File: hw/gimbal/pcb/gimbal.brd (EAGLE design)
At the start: 60 x 40 mm, 43 parts

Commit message: Progress on gimbal board.
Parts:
- added C14, C15: 0.01uF, rcl:C0603
- added C16, C17, C20, C21, C22, C23, C24: 0.1uF, rcl:C0603
- added C18, C19: 4.7uF, rcl:C0603
- added C25, C26: 10pF, rcl:C0603
- added R10, R8: 100k, rcl:R0603
- added R11, R9: 10k, rcl:R0603
- added R7: 10, rcl:R0603
- added U$16: (no value), gimbal:CRYSTAL-OSC-SMD-5X3.2
- U$14: value (none) -> 2.2uH
- moved PIMU 12.5 mm to (2.50, 29.0), turned to 270 degrees
- moved PABS 8.56 mm to (2.50, 18.5), turned to 270 degrees
- moved SIMU 2.24 mm to (2.50, 8.00), turned to 270 degrees
- moved U$9 1.97 mm to (8.50, 18.3), turned to 270 degrees
- moved R3 1.60 mm to (50.4, 20.2), turned to 180 degrees
- moved C7 1.50 mm to (38.0, 29.0)
- moved USBO 1.40 mm to (32.0, 24.1)
- moved JP3 1.12 mm to (12.3, 5.50)
- moved JP2 1.02 mm to (38.5, 1.80)
- moved C11 0.85 mm to (45.8, 24.7)
- moved R4 0.78 mm to (48.1, 23.5)
- moved C6 0.70 mm to (42.2, 34.7)
- moved C12 0.58 mm to (50.5, 27.0)
- moved JP1 0.54 mm to (56.0, 1.80)
- moved U$10 0.50 mm to (5.10, 37.3)
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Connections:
- new net BLDC_FAULT1: U$1.51, U$5.18
- new net BLDC_FAULT2: U$1.40, U$6.18
- new net BLDC_RESET/: U$1.4, U$5.16, U$6.16
- new net BLDC_SLEEP/: U$1.3, U$5.17, U$6.17
- new net MOTOR1_EN: U$5.22, U$5.24, U$5.26
- new net MOTOR1_IN1: U$1.37, U$5.27
- new net MOTOR1_IN2: U$1.38, U$5.25
- new net MOTOR1_IN3: U$1.39, U$5.23
- new net MOTOR2_EN: U$6.22, U$6.24, U$6.26
- new net MOTOR2_IN1: U$1.14, U$6.27
- new net MOTOR2_IN2: U$1.15, U$6.25
- new net MOTOR2_IN3: U$1.16, U$6.23
- new net N$23: C18.1, U$1.30
- new net N$24: C24.1, U$1.7, U$9.5
- new net N$25: C14.1, U$6.1
- new net N$26: C14.2, U$6.2
- new net N$27: C15.2, U$5.2
- new net N$28: C15.1, U$5.1
- new net N$29: C16.2, U$5.3
- new net N$30: C17.2, U$6.3
- new net N$31: U$1.49, U$9.2
- new net N$32: U$1.46, U$9.4
- new net N$33: R7.2, U$1.60
- new net N$34: R8.1, R9.2, U$1.9
- new net N$35: C25.1, U$1.5, U$16.1
- new net N$36: C26.1, U$1.6, U$16.3
- new net N$38: R10.1, R11.2, U$1.10
- new net SLAVE_RX: U$1.55, U$8.3
- new net SLAVE_TX: U$1.50, U$8.2
- net +12V: now also C16.1, C17.1, R10.2, U$5.11, U$5.4, U$6.11, U$6.4
- net +3V3: now also C19.1, C20.1, C21.1, C22.1, C23.1, JP3.5, U$1.1, U$1.13, U$1.19, U$1.32, U$1.48, U$1.64, U$9.1
- net +8V: now also R8.2, U$8.4
- net AEG_PWM: now also U$1.26
- net AGITATOR_PWM: now also U$1.27
- net BOOST_EN: now also U$1.52
- net GND: now also C18.2, C19.2, C20.2, C21.2, C22.2, C23.2, C24.2, C25.2, C26.2, R11.1, R7.1, R9.1, U$1.31, U$1.47, U$16.2, U$16.4, U$5.10, U$5.14, U$5.20, U$5.28, U$5.6, U$5.7, U$5.G0, U$5.G1, U$5.G2, U$5.G3, U$5.G4, U$5.G5, U$5.G6, U$5.G7, U$5.G8, U$6.10, U$6.14, U$6.20, U$6.28, U$6.6, U$6.7, U$6.G0, U$6.G1, U$6.G2, U$6.G3, U$6.G4, U$6.G5, U$6.G6, U$6.G7, U$6.G8, U$8.1, U$9.3
- net LASER_EN: now also U$1.28
- net MOTOR_D1: now also U$1.53
- net MOTOR_FB: now also U$1.8
- net MOTOR_SF: now also U$1.2
- net PABS_SCL: now also U$1.41; no longer U$1.61
- net PABS_SDA: now also U$1.61; no longer U$1.62
- net PIMU_SCL: now also U$1.58; no longer U$1.41
- net PIMU_SDA: now also U$1.59; no longer U$1.40
- net SIMU_SDA: now also U$1.62; no longer U$1.55
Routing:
- added copper zone on layer 16, net GND

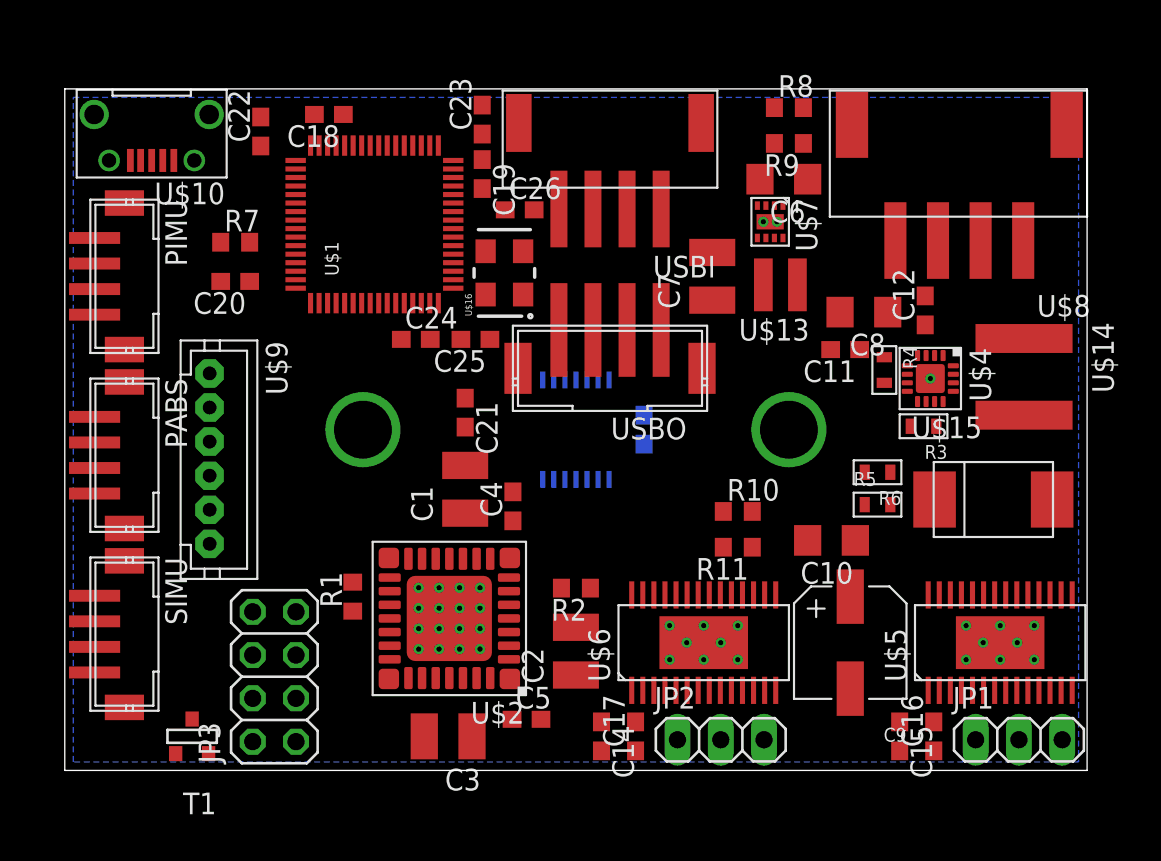
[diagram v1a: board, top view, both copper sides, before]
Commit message: gimbal board: Fix all DRC errors with part placement and library.
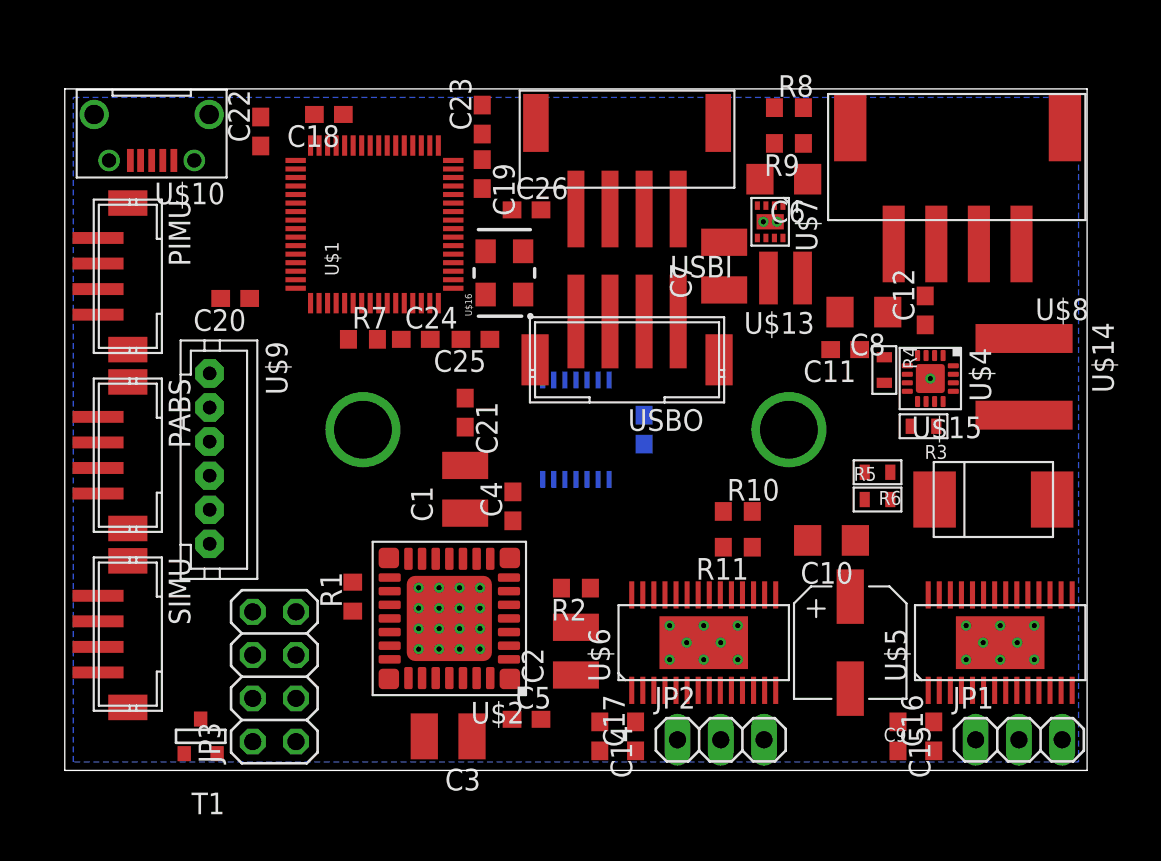
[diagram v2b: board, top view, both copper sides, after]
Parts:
- moved R7 9.42 mm to (17.5, 25.3)
- moved USBO 1.12 mm to (33.0, 24.6)
- moved C20 1.00 mm to (10.0, 27.7)
- moved USBI 1.00 mm to (33.0, 35.7)
- moved C7 0.92 mm to (38.7, 29.6)
- moved T1 0.50 mm to (8.00, 2.00)
- moved U$13 0.50 mm to (42.3, 28.9)
- moved C26 0.40 mm to (27.1, 32.9)
- moved R5 0.30 mm to (47.7, 15.9)
- moved U$8 0.22 mm to (52.4, 35.5)
- moved PABS 0.20 mm to (2.70, 18.5)
- moved PIMU 0.20 mm to (2.70, 29.0)
- moved SIMU 0.20 mm to (2.70, 8.00)
- moved C14 0.10 mm to (31.4, 2.00)
- moved C15 0.10 mm to (48.9, 2.00)

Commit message: gimbal board: Continued work: Updated all resistors and caps to the MF libraries.
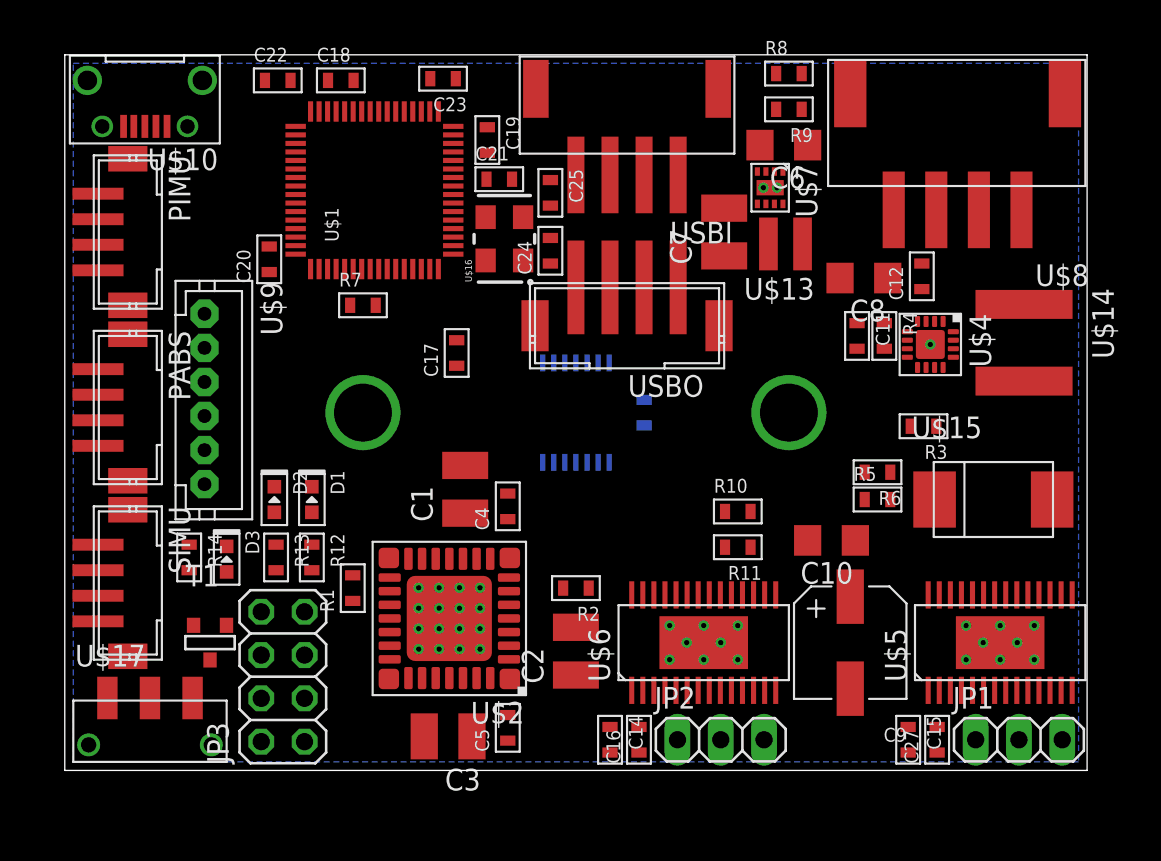
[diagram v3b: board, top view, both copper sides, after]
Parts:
- removed C26: 10pF, rcl:C0603
- added C27: 0.1uF, mfpassives:C0603
- added D1, D2, D3: (no value), mfleds:LED0603
- added R12, R13, R14: 560, mfpassives:R0603
- added U$17: SLIDE_SWITCHJS_SUB_SWITCH, gimbal:JS_SUB_SWITCH
- C11, C12, C13, C14, C15, C16, C17, C18, C19, C20, C21, C22, C23, C25, C4, C5: device rcl:C0603 -> mfpassives:C0603
- C24: value 0.1uF -> 10pF; device rcl:C0603 -> mfpassives:C0603
- R1, R10, R11, R2, R7, R8, R9: device rcl:R0603 -> mfpassives:R0603
- moved C17 24.8 mm to (23.0, 24.5)
- moved C16 17.3 mm to (33.7, 1.80)
- moved C21 13.8 mm to (25.5, 34.7), turned to 0 degrees
- moved C25 9.66 mm to (28.5, 33.9), turned to 270 degrees
- moved C24 9.46 mm to (28.5, 30.5), turned to 90 degrees
- moved T1 5.52 mm to (8.50, 7.50), turned to 0 degrees
- moved U$9 3.51 mm to (8.20, 21.8)
- moved C23 3.32 mm to (22.2, 40.6), turned to 180 degrees
- moved C22 3.16 mm to (12.5, 40.5), turned to 0 degrees
- moved C20 3.05 mm to (12.0, 30.0), turned to 90 degrees
- moved SIMU 3.00 mm to (2.70, 11.0)
- moved PABS 2.80 mm to (2.70, 21.3)
- moved PIMU 2.60 mm to (2.70, 31.6)
- moved C18 2.12 mm to (16.2, 40.5), turned to 0 degrees
- moved U$10 2.04 mm to (4.70, 39.3)
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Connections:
- new net N$37: D2.CATHODE, U$1.35
- new net N$39: D1.ANODE, R12.P$1
- new net N$40: D2.ANODE, R13.P$1
- new net N$41: D3.ANODE, R14.P$1
- new net N$42: D3.CATHODE, U$1.34
- new net N$43: D1.CATHODE, U$1.36
- net +12V: now also C16.P$1, C27.P$1, R10.P$2; no longer C16.1, C17.1, R10.2
- net +3V3: now also C13.P$1, C17.P$1, C19.P$1, C20.P$1, C22.P$1, C23.P$1, R1.P$2, R12.P$2, R13.P$2, R14.P$2, U$17.1; no longer C13.1, C19.1, C20.1, C21.1, C22.1, C23.1, R1.2
- net +8V: now also R8.P$2; no longer R8.2
- net GND: now also C11.P$2, C12.P$2, C13.P$2, C17.P$2, C18.P$2, C19.P$2, C20.P$2, C21.P$2, C22.P$2, C23.P$2, C24.P$2, C25.P$2, C4.P$2, R11.P$1, R2.P$1, R7.P$1, R9.P$1, U$17.3; no longer C11.2, C12.2, C13.2, C18.2, C19.2, C20.2, C21.2, C22.2, C23.2, C24.2, C25.2, C26.2, C4.2, R11.1, R2.1, R7.1, R9.1
- net MOTOR_EN: now also U$1.33, U$17.2
- net MOTOR_FB: now also R2.P$2; no longer R2.2
- net MOTOR_SF: now also R1.P$1; no longer R1.1
- net N$19: now also C11.P$1; no longer C11.1
- net N$21: now also C12.P$1; no longer C12.1
- net N$23: now also C18.P$1; no longer C18.1
- net N$24: now also C21.P$1; no longer C24.1
- net N$25: now also C14.P$1; no longer C14.1
- net N$26: now also C14.P$2; no longer C14.2
- net N$27: now also C15.P$2; no longer C15.2
- net N$28: now also C15.P$1; no longer C15.1
- net N$29: now also C27.P$2; no longer C16.2
- net N$30: now also C16.P$2; no longer C17.2
- net N$33: now also R7.P$2; no longer R7.2
- net N$34: now also R8.P$1, R9.P$2; no longer R8.1, R9.2
- net N$35: now also C24.P$1; no longer C25.1
- net N$36: now also C25.P$1; no longer C26.1
- net N$38: now also R10.P$1, R11.P$2; no longer R10.1, R11.2
- net N$4: now also C4.P$1, C5.P$1; no longer C4.1, C5.1
- net N$5: now also C5.P$2; no longer C5.2
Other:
- board size 60 x 40 mm -> 60 x 42 mm

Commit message: gimbal board: Finish updating the remaining larger caps to the macrofab library versions.
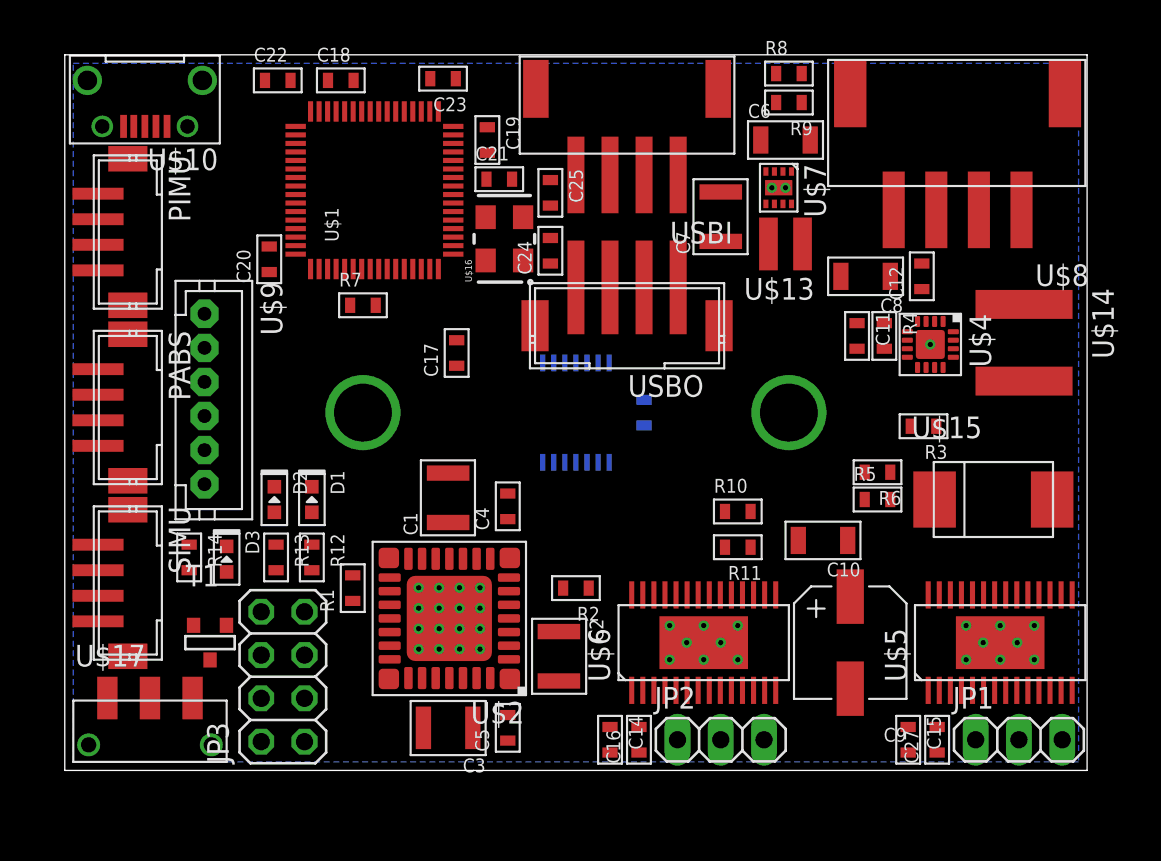
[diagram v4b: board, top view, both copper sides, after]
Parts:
- C1, C2, C3, C7: device rcl:C1210 -> mfpassives:C1210
- C10, C6, C8: device rcl:C1206 -> mfpassives:C1206
- moved C1 1.12 mm to (22.5, 16.0)
- moved C2 1.04 mm to (29.0, 6.70), turned to 270 degrees
- moved C7 0.92 mm to (38.5, 32.5)
- moved C10 0.50 mm to (44.5, 13.5)
- moved C3 0.50 mm to (22.5, 2.50)
- moved U$7 0.50 mm to (41.9, 34.2)
- moved R9 0.40 mm to (42.5, 39.2)
- moved C6 0.32 mm to (42.3, 37.0), turned to 0 degrees
- moved C8 0.14 mm to (47.0, 29.0)
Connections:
- net +12V: now also C10.P$1; no longer C10.1
- net +3V3: now also C7.P$1; no longer C7.1
- net +8V: now also C6.P$1, C8.P$1; no longer C6.1, C8.1
- net GND: now also C1.P$2, C10.P$2, C2.P$2, C3.P$2, C6.P$2, C7.P$2, C8.P$2; no longer C1.2, C10.2, C2.2, C3.2, C6.2, C7.2, C8.2
- net N$4: now also C1.P$1, C2.P$1, C3.P$1; no longer C1.1, C2.1, C3.1

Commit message: gimbal board: Select a few parts, update TODO.
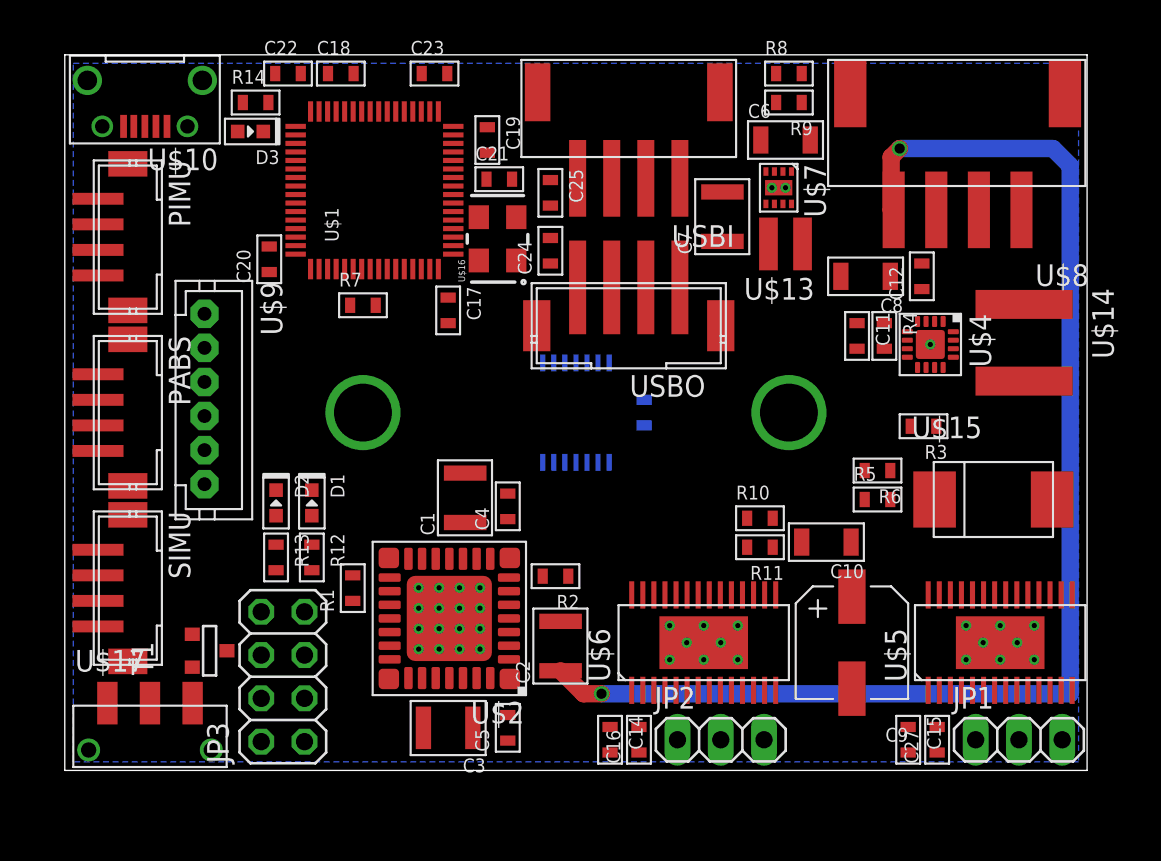
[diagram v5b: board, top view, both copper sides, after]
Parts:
- moved R14 27.0 mm to (11.2, 39.2), turned to 0 degrees
- moved D3 25.1 mm to (10.9, 37.5), turned to 180 degrees
- moved C17 2.55 mm to (22.5, 27.0), turned to 270 degrees
- moved R2 1.39 mm to (28.8, 11.4)
- moved R10 1.36 mm to (40.8, 14.8)
- moved R11 1.30 mm to (40.8, 13.1)
- moved C1 1.00 mm to (23.5, 16.0)
- moved C22 0.72 mm to (13.1, 40.9)
- moved C2 0.61 mm to (29.1, 7.30), turned to 90 degrees
- moved C23 0.58 mm to (21.7, 40.9), turned to 0 degrees
- moved T1 0.50 mm to (8.50, 7.00), turned to 90 degrees
- moved U$16 0.40 mm to (25.4, 31.2)
- moved C18 0.40 mm to (16.2, 40.9)
- moved PABS 0.30 mm to (2.70, 21.0)
- moved PIMU 0.30 mm to (2.70, 31.3)
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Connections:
- removed net N$4: C1.P$1, C2.P$1, C3.P$1, C4.P$1, C5.P$1, U$2.11, U$2.31, U$2.4, U$2.6
- net +8V: now also C1.P$1, C2.P$1, C3.P$1, C4.P$1, C5.P$1, U$2.11, U$2.31, U$2.4, U$2.6
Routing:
- net +8V: track 0.00 -> 75.8 mm, vias 0 -> 2

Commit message: gimbal board: I2C pullups, AS50448A CS line, and more vias under the 12V boost regulator.
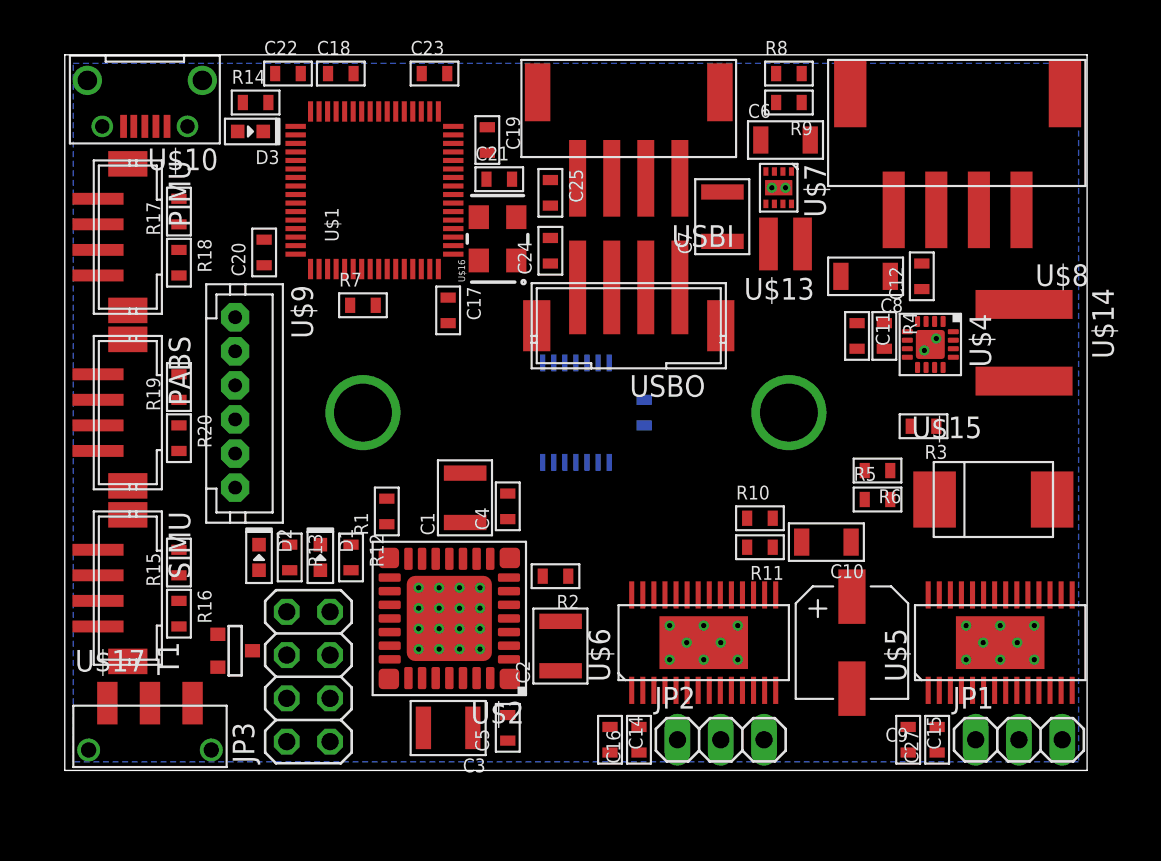
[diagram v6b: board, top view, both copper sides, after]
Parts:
- added R15, R16, R17, R18, R19, R20: 1.69k, mfpassives:R0603
- moved R1 4.92 mm to (18.9, 15.2)
- moved D2 3.35 mm to (11.4, 12.5)
- moved D1 3.24 mm to (15.0, 12.5)
- moved R12 2.30 mm to (16.8, 12.5)
- moved U$9 1.81 mm to (10.0, 21.6)
- moved JP3 1.50 mm to (14.3, 5.50)
- moved T1 1.50 mm to (10.0, 7.00)
- moved R13 0.80 mm to (13.2, 12.5)
- moved C20 0.50 mm to (11.7, 30.4)
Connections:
- new net AS5048_CS: U$1.20, U$3.1
- net +3V3: now also R15.P$2, R16.P$2, R17.P$2, R18.P$2, R19.P$2, R20.P$2
- net GND: now also U$4.G2
- net PABS_SCL: now also R20.P$1
- net PABS_SDA: now also R19.P$1
- net PIMU_SCL: now also R18.P$1
- net PIMU_SDA: now also R17.P$1
- net SIMU_SCL: now also R16.P$1
- net SIMU_SDA: now also R15.P$1
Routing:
- net +8V: track 75.8 -> 0.00 mm, vias 2 -> 0
